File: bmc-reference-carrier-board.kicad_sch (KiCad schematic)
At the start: 0 parts

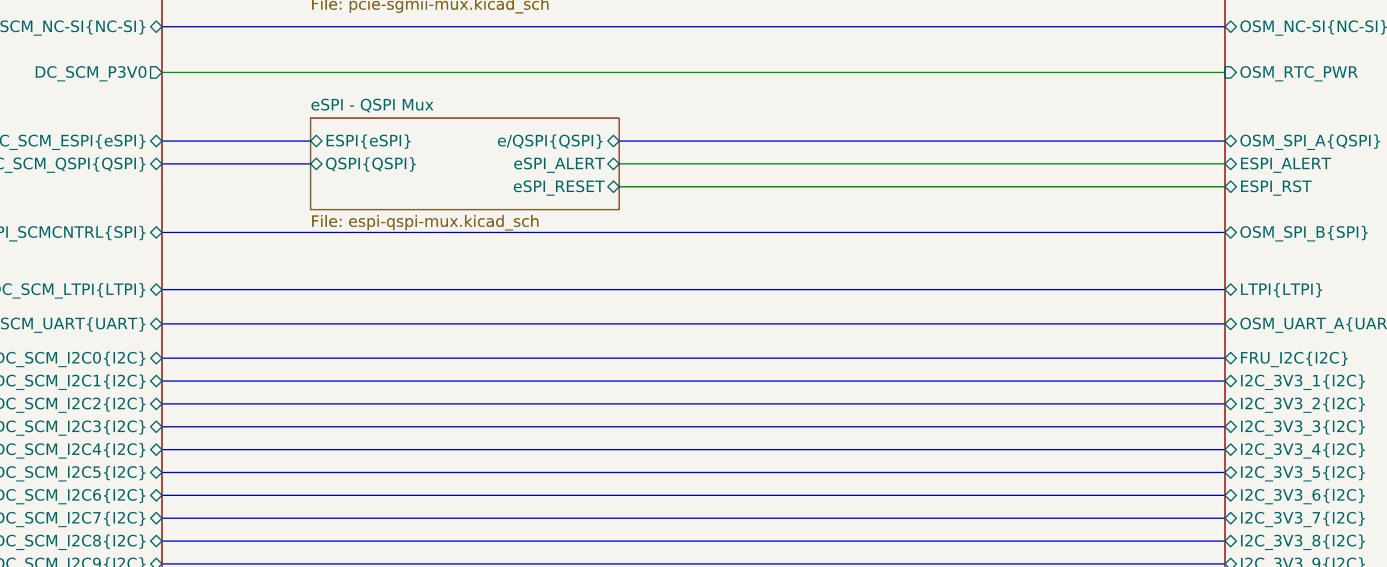
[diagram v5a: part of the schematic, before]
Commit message: [#83146] Fix LTPI connection, add bias
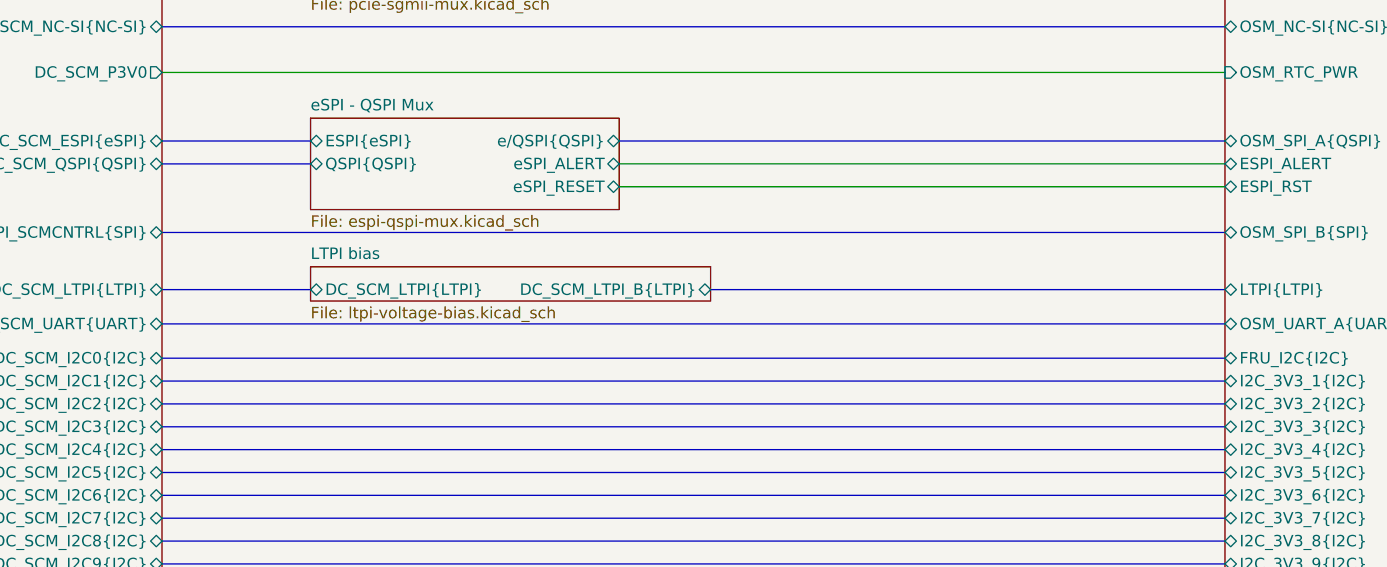
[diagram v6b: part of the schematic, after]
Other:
- added sheet LTPI bias (ltpi-voltage-bias.kicad_sch)
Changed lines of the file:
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@@
-	(bus
-		(pts
-			(xy 176.53 194.31) (xy 58.42 194.31)
-		)
-		(stroke
-			(width 0)
-			(type default)
-		)
-	)
 	(bus
 		(pts
@@
 	(bus
 		(pts
+			(xy 58.42 194.31) (xy 74.93 194.31)
+		)
+		(stroke
+			(width 0)
+			(type default)
+		)
+	)
+	(bus
+		(pts
 			(xy 251.46 186.69) (xy 289.56 186.69)
 		)
@@
 		(pts
 			(xy 58.42 240.03) (xy 176.53 240.03)
+		)
+		(stroke
+			(width 0)
+			(type default)
+		)
+	)
+	(bus
+		(pts
+			(xy 119.38 194.31) (xy 176.53 194.31)
 		)
 		(stroke
@@
 				)
 			)
+		)
+	)
+	(sheet
+		(at 74.93 191.77)
+		(size 44.45 3.81)
+		(exclude_from_sim no)
+		(in_bom yes)
+		(on_board yes)
+		(dnp no)
+		(fields_autoplaced yes)
+		(stroke
+			(width 0.1524)
+			(type solid)
+		)
+		(fill
+			(color 0 0 0 0.0000)
+		)
+		(property "Sheetname" "LTPI bias"
+			(at 74.93 191.0584 0)
+			(effects
+				(font
+					(size 1.27 1.27)
+				)
+				(justify left bottom)
+			)
+		)
+		(property "Sheetfile" "ltpi-voltage-bias.kicad_sch"
+			(at 74.93 196.1646 0)
+			(effects
+				(font
+					(size 1.27 1.27)
+				)
+				(justify left top)
+			)
+		)
+		(pin "DC_SCM_LTPI_B{LTPI}" bidirectional
+			(at 119.38 194.31 0)
+			(effects
+				(font
+					(size 1.27 1.27)
+				)
+				(justify right)
+			)
+		)
+		(pin "DC_SCM_LTPI{LTPI}" bidirectional
+			(at 74.93 194.31 180)
+			(effects
+				(font
+					(size 1.27 1.27)
+				)
+				(justify left)
+			)
+		)
+		(instances
+			(project "bmc-reference-carrier-board"
+				(path "/5f636c45-3c15-4731-8931-4625e0dab7e4"
+					(page "18")
+				)
+			)

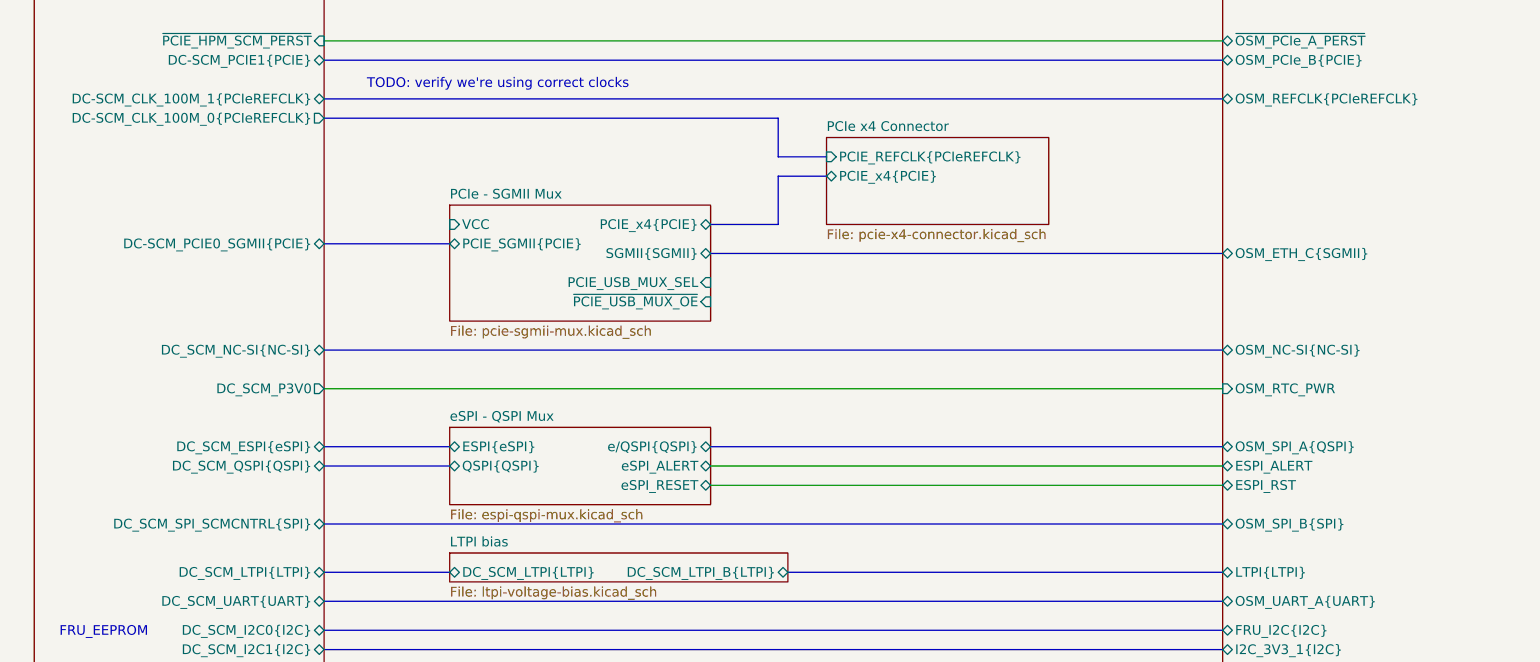
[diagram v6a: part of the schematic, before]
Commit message: [#82233] Added eSPI/QSPI mux and DNP QSPI flash memory
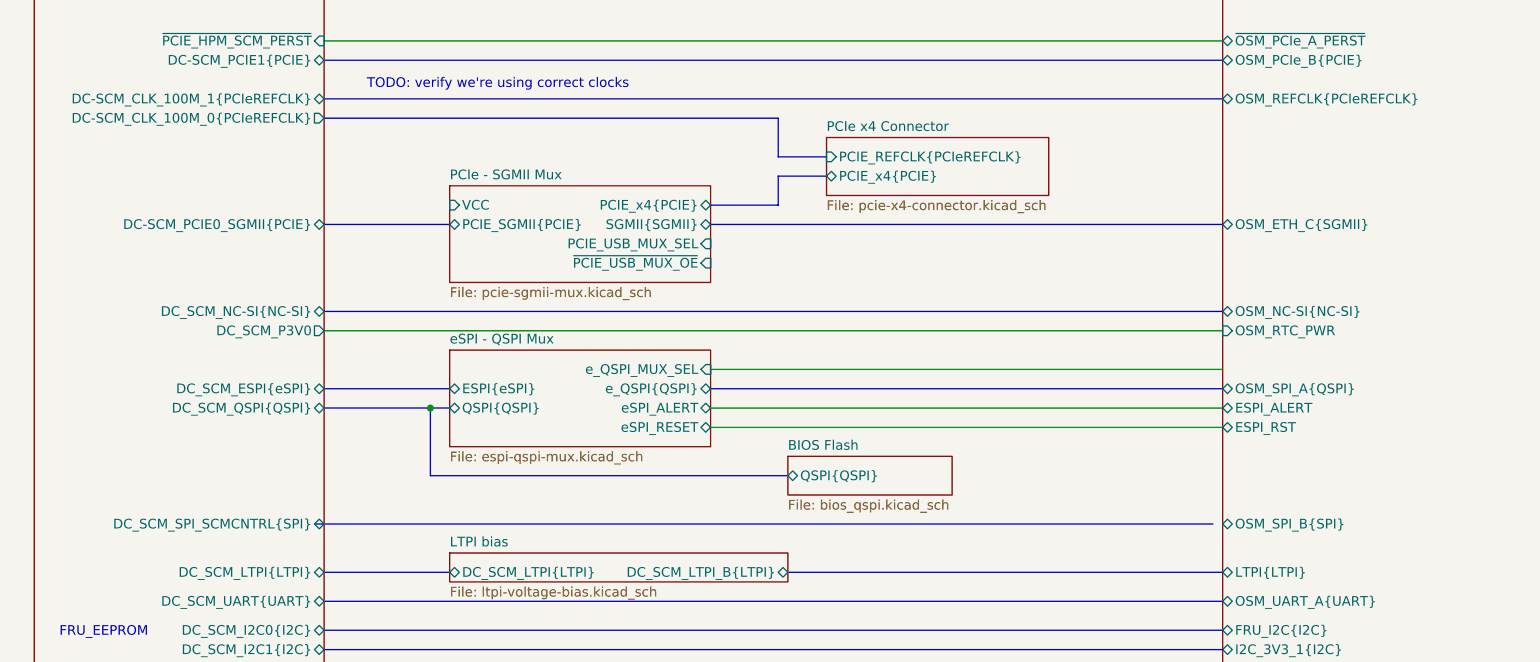
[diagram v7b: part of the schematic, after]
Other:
- added sheet BIOS Flash (bios_qspi.kicad_sch)
- sheet eSPI - QSPI Mux ports: added e_QSPI_MUX_SEL, e_QSPI{QSPI}; removed e/QSPI{QSPI}
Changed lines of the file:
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@@
 		)
+	)
+	(junction
+		(at 72.39 172.72)
+		(diameter 0)
+		(color 0 0 0 0)
 	)
 	(wire
@@
 	(wire
 		(pts
-			(xy 109.22 180.34) (xy 176.53 180.34)
+			(xy 109.22 172.72) (xy 176.53 172.72)
+		)
+		(stroke
+			(width 0)
+			(type default)
+		)
+	)
+	(bus
+		(pts
+			(xy 119.38 181.61) (xy 72.39 181.61)
 		)
 		(stroke
@@
 	(bus
 		(pts
-			(xy 58.42 177.8) (xy 74.93 177.8)
+			(xy 58.42 170.18) (xy 74.93 170.18)
 		)
 		(stroke
@@
 	(bus
 		(pts
-			(xy 58.42 187.96) (xy 176.53 187.96)
+			(xy 57.15 187.96) (xy 175.26 187.96)
 		)
 		(stroke
@@
 	(bus
 		(pts
-			(xy 118.11 148.59) (xy 118.11 142.24)
+			(xy 118.11 146.05) (xy 118.11 142.24)
 		)
 		(stroke
@@
 	(bus
 		(pts
-			(xy 58.42 151.13) (xy 74.93 151.13)
+			(xy 58.42 148.59) (xy 74.93 148.59)
 		)
 		(stroke
@@
 	(bus
 		(pts
+			(xy 72.39 172.72) (xy 74.93 172.72)
+		)
+		(stroke
+			(width 0)
+			(type default)
+		)
+	)
+	(bus
+		(pts
 			(xy 172.72 43.18) (xy 176.53 43.18)
 		)
@@
 		)
 	)
+	(wire
+		(pts
+			(xy 109.22 167.64) (xy 176.53 167.64)
+		)
+		(stroke
+			(width 0)
+			(type default)
+		)
+	)
 	(bus
 		(pts
@@
 	(wire
 		(pts
-			(xy 109.22 182.88) (xy 176.53 182.88)
+			(xy 109.22 175.26) (xy 176.53 175.26)
 		)
 		(stroke
@@
 	(bus
 		(pts
-			(xy 109.22 177.8) (xy 176.53 177.8)
+			(xy 109.22 170.18) (xy 176.53 170.18)
 		)
 		(stroke
@@
 	(bus
 		(pts
-			(xy 109.22 148.59) (xy 118.11 148.59)
+			(xy 109.22 146.05) (xy 118.11 146.05)
 		)
 		(stroke
@@
 	(bus
 		(pts
-			(xy 109.22 152.4) (xy 176.53 152.4)
-		)
-		(stroke
-			(width 0)
-			(type default)
-		)
-	)
-	(bus
-		(pts
-			(xy 58.42 165.1) (xy 176.53 165.1)
+			(xy 109.22 148.59) (xy 176.53 148.59)
+		)
+		(stroke
+			(width 0)
+			(type default)
+		)
+	)
+	(bus
+		(pts
+			(xy 58.42 160.02) (xy 176.53 160.02)
 		)
 		(stroke
@@
 	(wire
 		(pts
-			(xy 58.42 170.18) (xy 176.53 170.18)
+			(xy 58.42 162.56) (xy 176.53 162.56)
 		)
 		(stroke
@@
 	(bus
 		(pts
-			(xy 58.42 180.34) (xy 74.93 180.34)
+			(xy 58.42 172.72) (xy 72.39 172.72)
 		)
 		(stroke
@@
 		(pts
 			(xy 118.11 142.24) (xy 124.46 142.24)
+		)
+		(stroke
+			(width 0)
+			(type default)
+		)
+	)
+	(bus
+		(pts
+			(xy 72.39 181.61) (xy 72.39 172.72)
 		)
 		(stroke
@@
 		)
 		(pin "OSM_ETH_C{SGMII}" bidirectional
-			(at 176.53 152.4 180)
+			(at 176.53 148.59 180)
 			(effects
 				(font
@@
 		)
 		(pin "OSM_RTC_PWR" input
-			(at 176.53 170.18 180)
+			(at 176.53 162.56 180)
 			(effects
 				(font
@@
 		)
 		(pin "OSM_SPI_A{QSPI}" bidirectional
-			(at 176.53 177.8 180)
+			(at 176.53 170.18 180)
 			(effects
 				(font
@@
 		)
 		(pin "ESPI_ALERT" bidirectional
-			(at 176.53 180.34 180)
+			(at 176.53 172.72 180)
 			(effects
 				(font
@@
 		)
 		(pin "ESPI_RST" bidirectional
-			(at 176.53 182.88 180)
+			(at 176.53 175.26 180)
 			(effects
 				(font
@@
 		)
 		(pin "OSM_NC-SI{NC-SI}" bidirectional
-			(at 176.53 165.1 180)
+			(at 176.53 160.02 180)
 			(effects
 				(font
@@
 	(sheet
 		(at 124.46 137.16)
-		(size 29.21 11.43)
+		(size 29.21 7.62)
 		(exclude_from_sim no)
 		(in_bom yes)
@@
 		)
 		(property "Sheetfile" "pcie-x4-connector.kicad_sch"
-			(at 124.46 149.1746 0)
+			(at 124.46 145.3646 0)
 			(effects
 				(font
@@
 	)
 	(sheet
-		(at 74.93 146.05)
-		(size 34.29 15.24)
+		(at 74.93 143.51)
+		(size 34.29 12.7)
 		(exclude_from_sim no)
 		(in_bom yes)
@@
 		)
 		(property "Sheetname" "PCIe - SGMII Mux"
-			(at 74.93 145.3384 0)
+			(at 74.93 142.7984 0)
 			(effects
 				(font
@@
 		)
 		(property "Sheetfile" "pcie-sgmii-mux.kicad_sch"
-			(at 74.93 161.8746 0)
+			(at 74.93 156.7946 0)
 			(effects
 				(font
@@
 		)
 		(pin "PCIE_SGMII{PCIE}" bidirectional
-			(at 74.93 151.13 180)
+			(at 74.93 148.59 180)
 			(effects
 				(font
@@
 		)
 		(pin "SGMII{SGMII}" bidirectional
-			(at 109.22 152.4 0)
+			(at 109.22 148.59 0)
 			(effects
 				(font
@@
 		)
 		(pin "PCIE_x4{PCIE}" bidirectional
-			(at 109.22 148.59 0)
+			(at 109.22 146.05 0)
 			(effects
 				(font
@@
 		)
 		(pin "PCIE_USB_MUX_SEL" input
-			(at 109.22 156.21 0)
+			(at 109.22 151.13 0)
 			(effects
 				(font
@@
 		)
 		(pin "VCC" input
-			(at 74.93 148.59 180)
+			(at 74.93 146.05 180)
 			(effects
 				(font
@@
 		)
 		(pin "~{PCIE_USB_MUX_OE}" input
-			(at 109.22 158.75 0)
+			(at 109.22 153.67 0)
 			(effects
 				(font
@@
 		)
 		(pin "DC_SCM_QSPI{QSPI}" bidirectional
-			(at 58.42 180.34 0)
+			(at 58.42 172.72 0)
 			(effects
 				(font
@@
 		)
 		(pin "DC_SCM_P3V0" output
-			(at 58.42 170.18 0)
+			(at 58.42 162.56 0)
 			(effects
 				(font
@@
 		)
 		(pin "DC_SCM_ESPI{eSPI}" bidirectional
-			(at 58.42 177.8 0)
+			(at 58.42 170.18 0)
 			(effects
 				(font
@@
 		)
 		(pin "DC_SCM_NC-SI{NC-SI}" bidirectional
-			(at 58.42 165.1 0)
+			(at 58.42 160.02 0)
 			(effects
 				(font
@@
 		)
 		(pin "DC-SCM_PCIE0_SGMII{PCIE}" bidirectional
-			(at 58.42 151.13 0)
+			(at 58.42 148.59 0)
 			(effects
 				(font
@@
 	)
 	(sheet
-		(at 74.93 175.26)
-		(size 34.29 10.16)
+		(at 74.93 165.1)
+		(size 34.29 12.7)
 		(exclude_from_sim no)
 		(in_bom yes)
@@
 		)
 		(property "Sheetname" "eSPI - QSPI Mux"
-			(at 74.93 174.5484 0)
+			(at 74.93 164.3884 0)
 			(effects
 				(font
@@
 		)
 		(property "Sheetfile" "espi-qspi-mux.kicad_sch"
-			(at 74.93 186.0046 0)
+			(at 74.93 178.3846 0)
 			(effects
 				(font
@@
 		)
 		(pin "ESPI{eSPI}" bidirectional
-			(at 74.93 177.8 180)
-			(effects
-				(font
-					(size 1.27 1.27)
-				)
-				(justify left)
-			)
-		)
-		(pin "e{slash}QSPI{QSPI}" bidirectional
-			(at 109.22 177.8 0)
-			(effects
-				(font
-					(size 1.27 1.27)
-				)
-				(justify right)
+			(at 74.93 170.18 180)
+			(effects
+				(font
+					(size 1.27 1.27)
+				)
+				(justify left)
 			)
 		)
 		(pin "QSPI{QSPI}" bidirectional
-			(at 74.93 180.34 180)
+			(at 74.93 172.72 180)
 			(effects
 				(font
@@
 		)
 		(pin "eSPI_ALERT" bidirectional
-			(at 109.22 180.34 0)
+			(at 109.22 172.72 0)
 			(effects
 				(font
@@
 		)
 		(pin "eSPI_RESET" bidirectional
-			(at 109.22 182.88 0)
+			(at 109.22 175.26 0)
+			(effects
+				(font
+					(size 1.27 1.27)
+				)
+				(justify right)
+			)
+		)
+		(pin "e_QSPI_MUX_SEL" input
+			(at 109.22 167.64 0)
+			(effects
+				(font
+					(size 1.27 1.27)
+				)
+				(justify right)
+			)
+		)
+		(pin "e_QSPI{QSPI}" bidirectional
+			(at 109.22 170.18 0)
 			(effects
 				(font
@@
 				)
 			)
+		)
+	)
+	(sheet
+		(at 119.38 179.07)
+		(size 21.59 5.08)
+		(exclude_from_sim no)
+		(in_bom yes)
+		(on_board yes)
+		(dnp yes)
+		(fields_autoplaced yes)
+		(stroke
+			(width 0.1524)
+			(type solid)
+		)
+		(fill
+			(color 0 0 0 0.0000)
+		)
+		(property "Sheetname" "BIOS Flash"
+			(at 119.38 178.3584 0)
+			(effects
+				(font
+					(size 1.27 1.27)
+				)
+				(justify left bottom)
+			)
+		)
+		(property "Sheetfile" "bios_qspi.kicad_sch"
+			(at 119.38 184.7346 0)
+			(effects
+				(font
+					(size 1.27 1.27)
+				)
+				(justify left top)
+			)
+		)
+		(pin "QSPI{QSPI}" bidirectional
+			(at 119.38 181.61 180)
+			(effects
+				(font
+					(size 1.27 1.27)
+				)
+				(justify left)
+			)
+		)
+		(instances
+			(project "bmc-reference-carrier-board"
+				(path "/5f636c45-3c15-4731-8931-4625e0dab7e4"
+					(page "19")
+				)
+			)

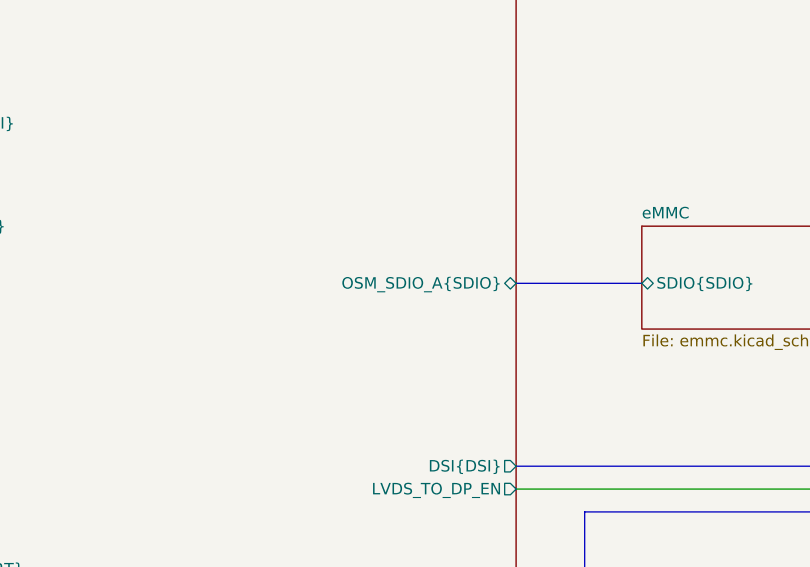
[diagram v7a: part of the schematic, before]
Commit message: [#82176] eMMC: change chip to 32GB & add decoupling
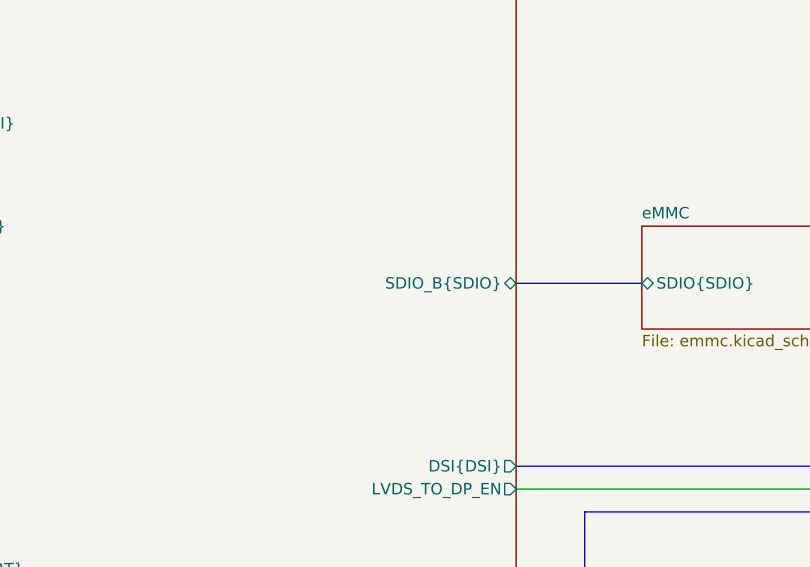
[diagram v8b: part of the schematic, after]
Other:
- sheet OSM L ports: added SDIO_B{SDIO}; removed OSM_SDIO_A{SDIO}
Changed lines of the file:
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@@
 	)
 	(bus_alias "SDIO"
-		(members "DAT[0..7]" "CMD" "CLK" "STRB" "~{RST}" "CD")
+		(members "DAT[0..7]" "CMD" "CLK" "~{CD}" "IOPWR" "PWR_EN" "WP" "DS")
 	)
 	(bus_alias "SGMII"
@@
 			)
 		)
-		(pin "OSM_SDIO_A{SDIO}" bidirectional
+		(pin "SDIO_B{SDIO}" bidirectional
 			(at 251.46 166.37 0)
 			(effects
